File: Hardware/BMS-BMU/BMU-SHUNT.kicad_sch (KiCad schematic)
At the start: 0 parts

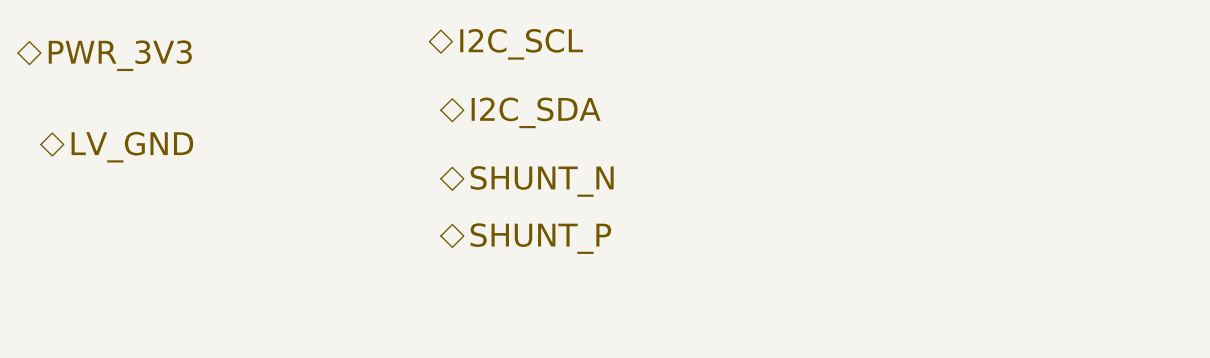
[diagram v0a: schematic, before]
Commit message: update CAN and SHUNT IF
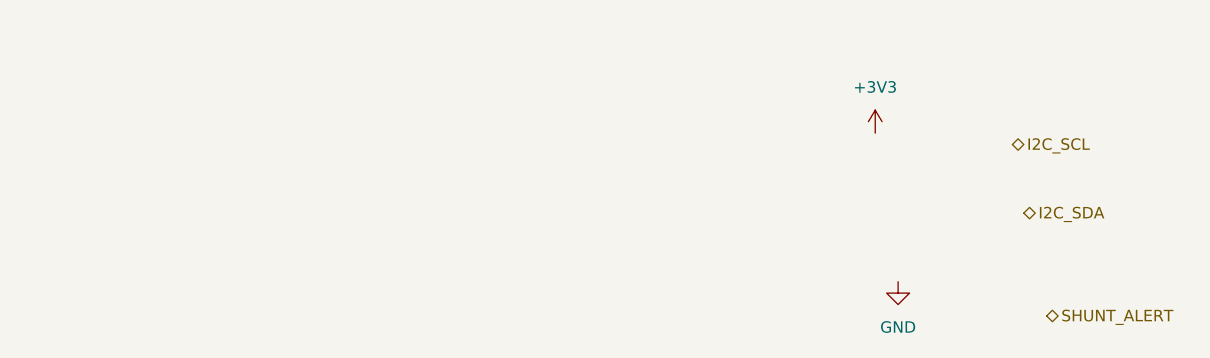
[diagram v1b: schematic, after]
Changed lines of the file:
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@@
 		(company "VIKING MOTOR SPORTS (VMS)")
 	)
-	(hierarchical_label "SHUNT_N"
+	(hierarchical_label "SHUNT_ALERT"
 		(shape bidirectional)
-		(at 148.59 76.2 0)
+		(at 215.9 91.44 0)
 		(effects
 			(font
-				(size 2.54 2.54)
-			)
-			(justify left)
-		)
-	)
-	(hierarchical_label "PWR_3V3"
-		(shape bidirectional)
-		(at 101.6 62.23 0)
-		(effects
-			(font
-				(size 2.54 2.54)
-			)
-			(justify left)
-		)
-	)
-	(hierarchical_label "LV_GND"
-		(shape bidirectional)
-		(at 104.14 72.39 0)
-		(effects
-			(font
-				(size 2.54 2.54)
+				(size 1.27 1.27)
 			)
 			(justify left)
@@
 	(hierarchical_label "I2C_SCL"
 		(shape bidirectional)
-		(at 147.32 60.96 0)
+		(at 212.09 72.39 0)
 		(effects
 			(font
-				(size 2.54 2.54)
+				(size 1.27 1.27)
 			)
 			(justify left)
@@
 	(hierarchical_label "I2C_SDA"
 		(shape bidirectional)
-		(at 148.59 68.58 0)
+		(at 213.36 80.01 0)
 		(effects
 			(font
-				(size 2.54 2.54)
+				(size 1.27 1.27)
 			)
 			(justify left)
 		)
 	)
-	(hierarchical_label "SHUNT_P"
-		(shape bidirectional)
-		(at 148.59 82.55 0)
-		(effects
-			(font
-				(size 2.54 2.54)
+	(symbol
+		(lib_id "power:GND")
+		(at 199.39 87.63 0)
+		(unit 1)
+		(body_style 1)
+		(exclude_from_sim no)
+		(in_bom yes)
+		(on_board yes)
+		(in_pos_files yes)
+		(dnp no)
+		(fields_autoplaced yes)
+		(property "Reference" "#PWR025"
+			(at 199.39 93.98 0)
+			(hide yes)
+			(show_name no)
+			(do_not_autoplace no)
+			(effects
+				(font
+					(size 1.27 1.27)
+				)
 			)
-			(justify left)
+		)
+		(property "Value" "GND"
+			(at 199.39 92.71 0)
+			(show_name no)
+			(do_not_autoplace no)
+			(effects
+				(font
+					(size 1.27 1.27)
+				)
+			)
+		)
+		(property "Footprint" ""
+			(at 199.39 87.63 0)
+			(hide yes)
+			(show_name no)
+			(do_not_autoplace no)
+			(effects
+				(font
+					(size 1.27 1.27)
+				)
+			)
+		)
+		(property "Datasheet" ""
+			(at 199.39 87.63 0)
+			(hide yes)
+			(show_name no)
+			(do_not_autoplace no)
+			(effects
+				(font
+					(size 1.27 1.27)
+				)
+			)
+		)
+		(property "Description" "Power symbol creates a global label with name \"GND\" , ground"
+			(at 199.39 87.63 0)
+			(hide yes)
+			(show_name no)
+			(do_not_autoplace no)
+			(effects
+				(font
+					(size 1.27 1.27)
+				)
+			)
+		)
+		(pin "1"
+		)
+		(instances
+			(project "BMS"
+				(path "/efb70416-ce55-4766-98ba-c3d23efcccb1/a5244361-9b33-4184-ac70-90b0e1995dcc"
+					(reference "#PWR025")
+					(unit 1)
+				)
+			)
 		)
 	)
+	(symbol
+		(lib_id "power:+3V3")
+		(at 196.85 71.12 0)
+		(unit 1)
+		(body_style 1)
+		(exclude_from_sim no)
+		(in_bom yes)
+		(on_board yes)
+		(in_pos_files yes)
+		(dnp no)
+		(fields_autoplaced yes)
+		(property "Reference" "#PWR09"
+			(at 196.85 74.93 0)
+			(hide yes)
+			(show_name no)
+			(do_not_autoplace no)
+			(effects
+				(font
+					(size 1.27 1.27)
+				)
+			)
+		)
+		(property "Value" "+3V3"
+			(at 196.85 66.04 0)
+			(show_name no)
+			(do_not_autoplace no)
+			(effects
+				(font
+					(size 1.27 1.27)
+				)
+			)
+		)
+		(property "Footprint" ""
+			(at 196.85 71.12 0)
+			(hide yes)
+			(show_name no)
+			(do_not_autoplace no)
+			(effects
+				(font
+					(size 1.27 1.27)
+				)
+			)
+		)
+		(property "Datasheet" ""
+			(at 196.85 71.12 0)
+			(hide yes)
+			(show_name no)
+			(do_not_autoplace no)
+			(effects
+				(font
+					(size 1.27 1.27)
+				)
+			)
+		)
+		(property "Description" "Power symbol creates a global label with name \"+3V3\""
+			(at 196.85 71.12 0)
+			(hide yes)
+			(show_name no)
+			(do_not_autoplace no)
+			(effects
+				(font
+					(size 1.27 1.27)
+				)
+			)
+		)
+		(pin "1"
+		)
+		(instances
+			(project "BMS"
+				(path "/efb70416-ce55-4766-98ba-c3d23efcccb1/a5244361-9b33-4184-ac70-90b0e1995dcc"
+					(reference "#PWR09")
+					(unit 1)
+				)
+			)
+		)
+	)
